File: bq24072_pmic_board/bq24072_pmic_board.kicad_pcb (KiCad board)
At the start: 2 copper layers, 40 x 20 mm, 28 parts, among them J101 USB_B_Micro, J102 Battery, J103 Conn_01x04_Female, U101 BQ24072RGT, U102 AMS1117-3.3

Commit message: WIP
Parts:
- removed JP101, JP102: SolderJumper_2_Open, Jumper:SolderJumper-2_P1.3mm_Open_RoundedPad1.0x1.5mm
- added JP1: SolderJumper_2_Open, Jumper:SolderJumper-2_P1.3mm_Open_RoundedPad1.0x1.5mm, F.Cu at (128.4, 97.2)
- added JP2: SolderJumper_2_Open, Jumper:SolderJumper-2_P1.3mm_Open_RoundedPad1.0x1.5mm, F.Cu at (128.4, 82.8)
- moved TP103 11.4 mm to (146.0, 86.0)
- moved J102 4.88 mm to (144.0, 93.5), turned to 0 degrees
- moved TP105 1.80 mm to (152.0, 96.6)
- moved REF** 0.20 mm to (158.0, 97.0)
- moved REF** 0.20 mm to (158.0, 83.0)
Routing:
- net Net-(C102-Pad2): track 35.5 -> 32.1 mm, vias 6 -> 4
- net Net-(J101-Pad6): track 16.9 -> 19.3 mm
- net GND: track 22.5 -> 24.5 mm, vias 14 -> 15
- net 3V3: track 22.1 -> 23.9 mm
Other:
- board text added: "+"
- board text added: "BAT"
- board text added: "V1"
- board text removed: "v1"

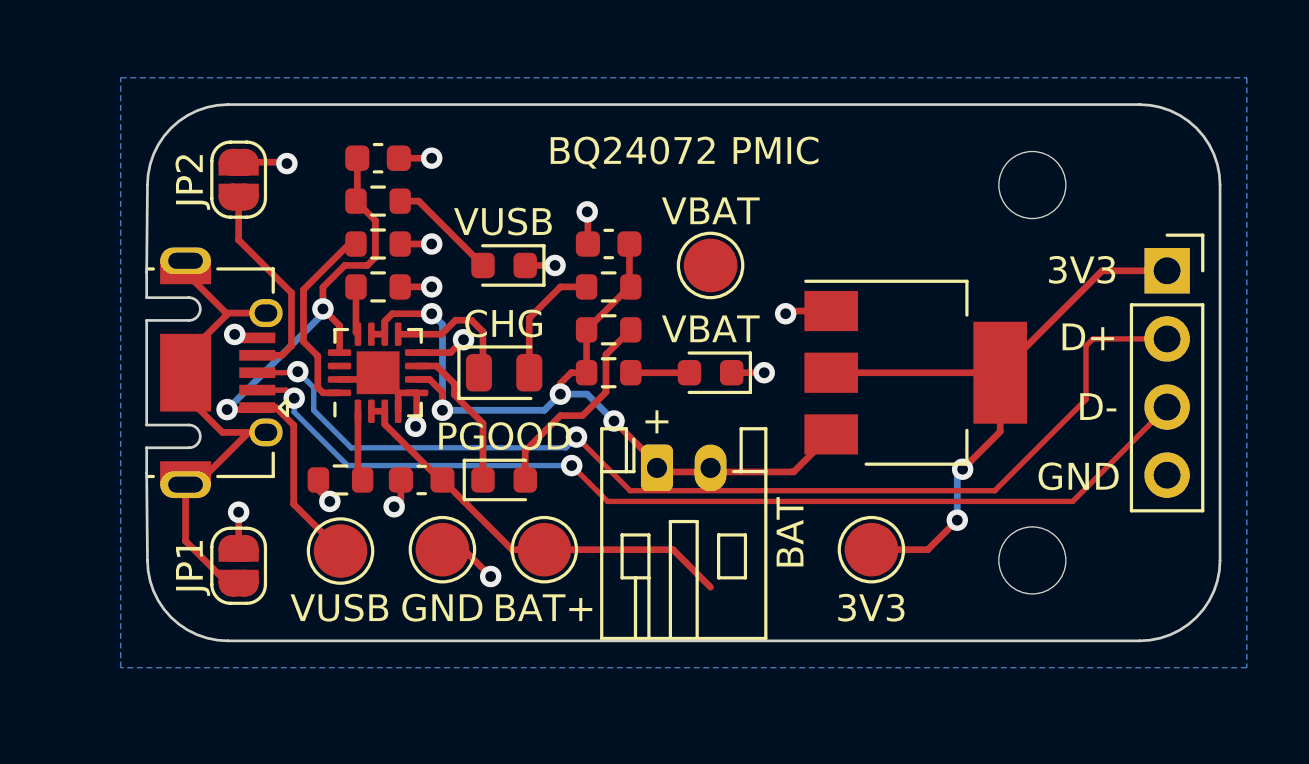
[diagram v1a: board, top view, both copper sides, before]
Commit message: [bq24072_pmic_board] Use hierarchical sheet for bq24072
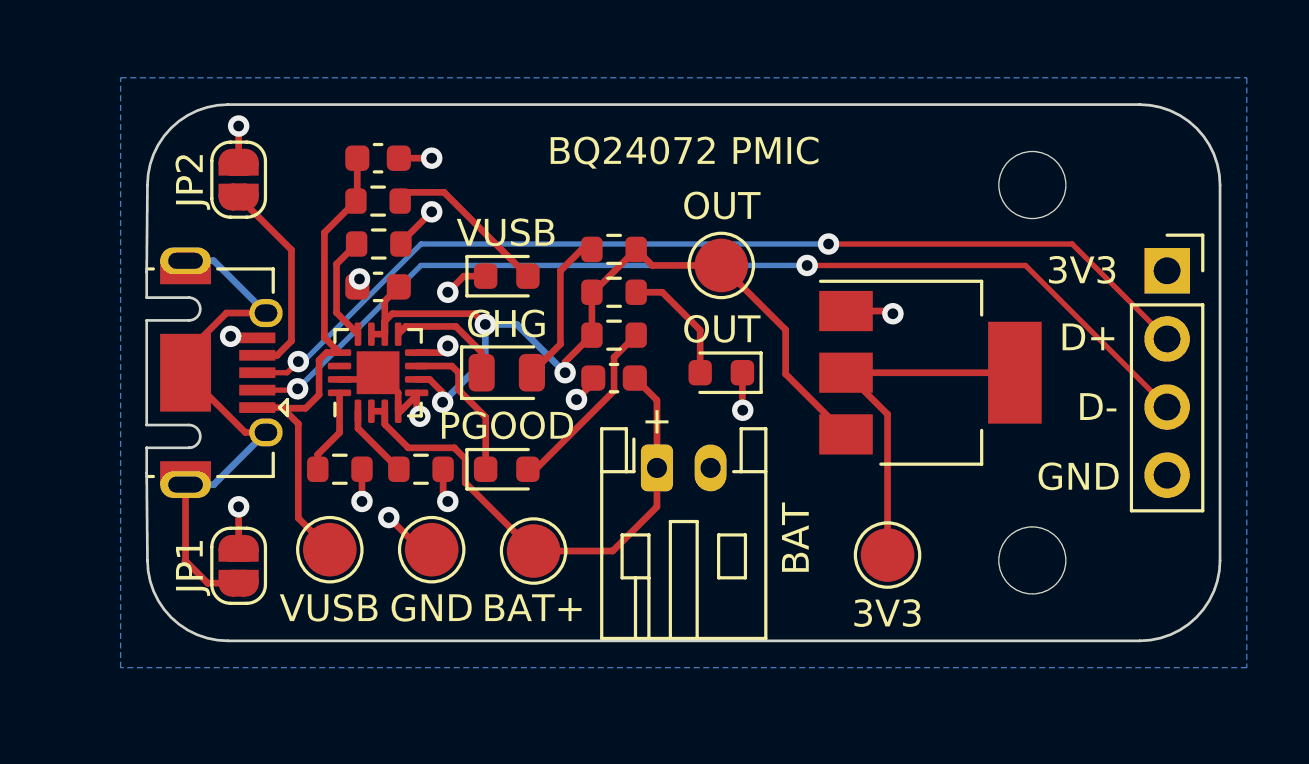
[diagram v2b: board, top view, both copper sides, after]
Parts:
- removed C101: 1u, Capacitor_SMD:C_0603_1608Metric
- removed C102, C103: 4.7u, Capacitor_SMD:C_0603_1608Metric
- removed D101: VUSB, LED_SMD:LED_0603_1608Metric
- removed D102: PGOOD, LED_SMD:LED_0603_1608Metric
- removed D103: CHG, LED_SMD:LED_0805_2012Metric
- removed D104: VBAT, LED_SMD:LED_0603_1608Metric
- removed R101: 180, Resistor_SMD:R_0603_1608Metric
- removed R102: 2k, Resistor_SMD:R_0603_1608Metric
- removed R103: 1k, Resistor_SMD:R_0603_1608Metric
- removed R104: 10k, Resistor_SMD:R_0603_1608Metric
- removed R105, R107: 47, Resistor_SMD:R_0603_1608Metric
- removed R106: 200, Resistor_SMD:R_0603_1608Metric
- removed TP105: 3V3, TestPoint:TestPoint_Pad_D2.0mm
- removed U102: AMS1117-3.3, Package_TO_SOT_SMD:SOT-223-3_TabPin2
- added C201: 1u, Capacitor_SMD:C_0603_1608Metric, F.Cu at (133.6, 82.0)
- added C202: 4.7u, Capacitor_SMD:C_0603_1608Metric, F.Cu at (133.6, 86.8)
- added C203: 4.7u, Capacitor_SMD:C_0603_1608Metric, F.Cu at (142.4, 90.2)
- added D201: VUSB, LED_SMD:LED_0603_1608Metric, F.Cu at (138.4, 86.4)
- added D202: PGOOD, LED_SMD:LED_0603_1608Metric, F.Cu at (138.4, 93.6)
- added D203: CHG, LED_SMD:LED_0805_2012Metric, F.Cu at (138.4, 90.0)
- added D204: OUT, LED_SMD:LED_0603_1608Metric, F.Cu at (146.4, 90.0)
- added R201: 180, Resistor_SMD:R_0603_1608Metric, F.Cu at (133.6, 83.6)
- added R202: 2k, Resistor_SMD:R_0603_1608Metric, F.Cu at (133.6, 85.2)
- added R203: 1k, Resistor_SMD:R_0603_1608Metric, F.Cu at (132.2, 93.6)
- added R204: 10k, Resistor_SMD:R_0603_1608Metric, F.Cu at (135.2, 93.6)
- added R205: 47, Resistor_SMD:R_0603_1608Metric, F.Cu at (142.4, 88.6)
- added R206: 200, Resistor_SMD:R_0603_1608Metric, F.Cu at (142.4, 85.4)
- added R207: 47, Resistor_SMD:R_0603_1608Metric, F.Cu at (142.4, 87.0)
- added TP201: VUSB, TestPoint:TestPoint_Pad_D2.0mm, F.Cu at (131.8, 96.6)
- added U201: BQ24072RGT, Package_DFN_QFN:VQFN-16-1EP_3x3mm_P0.5mm_EP1.6x1.6mm, F.Cu at (133.6, 90.0)
- TP101: value VUSB -> BAT+
- TP102: value BAT+ -> OUT
- TP103: value VBAT -> GND
- TP104: value GND -> 3V3
- U101: value BQ24072RGT -> AMS1117-3.3; footprint Package_DFN_QFN:VQFN-16-1EP_3x3mm_P0.5mm_EP1.6x1.6mm -> Package_TO_SOT_SMD:SOT-223-3_TabPin2
- moved U101 20.6 mm to (154.2, 90.0), turned to 0 degrees
- moved TP104 16.6 mm to (152.6, 96.8)
- moved TP103 14.8 mm to (135.6, 96.6), turned to 180 degrees
- moved TP102 12.5 mm to (146.4, 86.0)
- moved TP101 7.20 mm to (139.4, 96.7)
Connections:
- TP101 pad 1: VUSB -> BATT+
- TP102 pad 1: BATT+ -> OUT
- TP103 pad 1: Net-(C102-Pad2) -> GND
- TP104 pad 1: GND -> Net-(TP104-Pad1)
- U101 pad 1: Net-(R104-Pad2) -> GND
- U101 pad 2: BATT+ -> Net-(TP104-Pad1)
- U101 pad 3: BATT+ -> OUT
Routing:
- net OUT: track 0.00 -> 32.8 mm, vias 0 -> 3
- net Net-(C102-Pad2): track 32.1 -> 0.00 mm, vias 4 -> 0
- net 3V3: track 23.9 -> 0.00 mm, vias 2 -> 0
- net Net-(TP104-Pad1): track 0.00 -> 13.7 mm
- net Net-(D102-Pad2): track 7.71 -> 0.00 mm
- net Net-(R103-Pad1): track 7.42 -> 0.00 mm
- net Net-(D202-Pad2): track 0.00 -> 6.84 mm
- net Net-(D201-Pad2): track 0.00 -> 6.19 mm
- net Net-(D203-Pad2): track 0.00 -> 5.75 mm
- net Net-(D102-Pad1): track 5.71 -> 0.00 mm
- net Net-(D202-Pad1): track 0.00 -> 5.69 mm
- net Net-(D103-Pad1): track 5.14 -> 0.00 mm
- net Net-(D103-Pad2): track 4.66 -> 0.00 mm
- net Net-(D204-Pad2): track 0.00 -> 4.56 mm
- net Net-(D203-Pad1): track 0.00 -> 4.39 mm
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
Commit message: [bq24072_pmic_board] Move some LEDs from the hierarchical sheet
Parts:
- removed D201: VUSB, LED_SMD:LED_0603_1608Metric
- removed D204: OUT, LED_SMD:LED_0603_1608Metric
- removed R201: 180, Resistor_SMD:R_0603_1608Metric
- removed R207: 47, Resistor_SMD:R_0603_1608Metric
- added D101: VUSB, LED_SMD:LED_0603_1608Metric, F.Cu at (138.4, 86.4)
- added D102: VBAT, LED_SMD:LED_0603_1608Metric, F.Cu at (146.4, 90.0)
- added R101: 180, Resistor_SMD:R_0603_1608Metric, F.Cu at (133.6, 83.6)
- added R102: 47, Resistor_SMD:R_0603_1608Metric, F.Cu at (142.4, 87.0)
- moved TP104 1.02 mm to (153.6, 96.6)
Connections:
- TP104 pad 1: Net-(TP104-Pad1) -> 3V3
- U101 pad 2: Net-(TP104-Pad1) -> 3V3
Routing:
- net 3V3: track 0.00 -> 21.5 mm, vias 0 -> 1
- net Net-(TP104-Pad1): track 13.7 -> 0.00 mm
- net Net-(D201-Pad2): track 6.19 -> 0.00 mm
- net Net-(D101-Pad2): track 0.00 -> 6.19 mm
- net Net-(D204-Pad2): track 4.56 -> 0.00 mm
- net Net-(D102-Pad2): track 0.00 -> 4.56 mm

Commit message: final touches + v1 jlcpcb fab files
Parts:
- removed TP201: VUSB, TestPoint:TestPoint_Pad_D2.0mm
- added TP105: VUSB, TestPoint:TestPoint_Pad_D2.0mm, F.Cu at (132.0, 96.6)
- D102: value VBAT -> OUT
- R101: value 180 -> 1k
- R102, R205: value 47 -> 1k
- R206: value 200 -> 1k

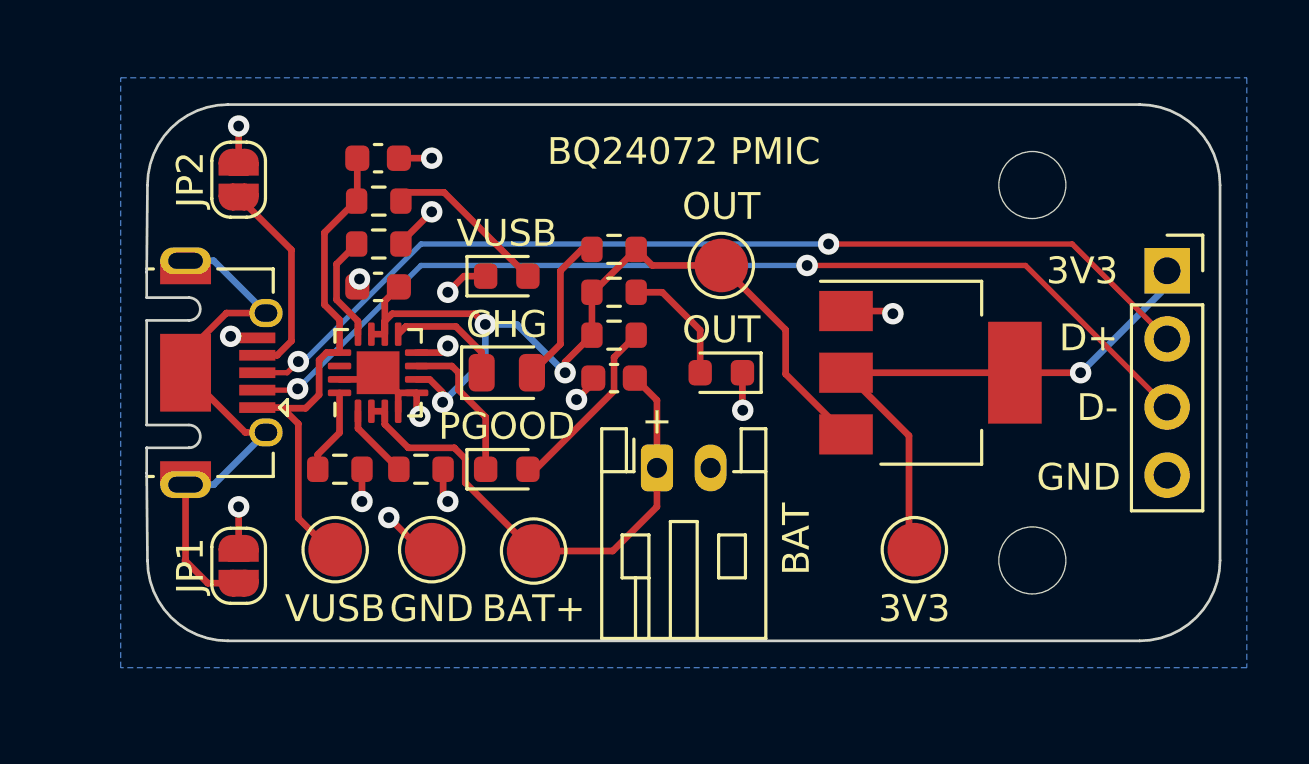
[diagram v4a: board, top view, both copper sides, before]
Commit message: [bq24072_pmic_board] Add VBUS output and bump board revision to v2
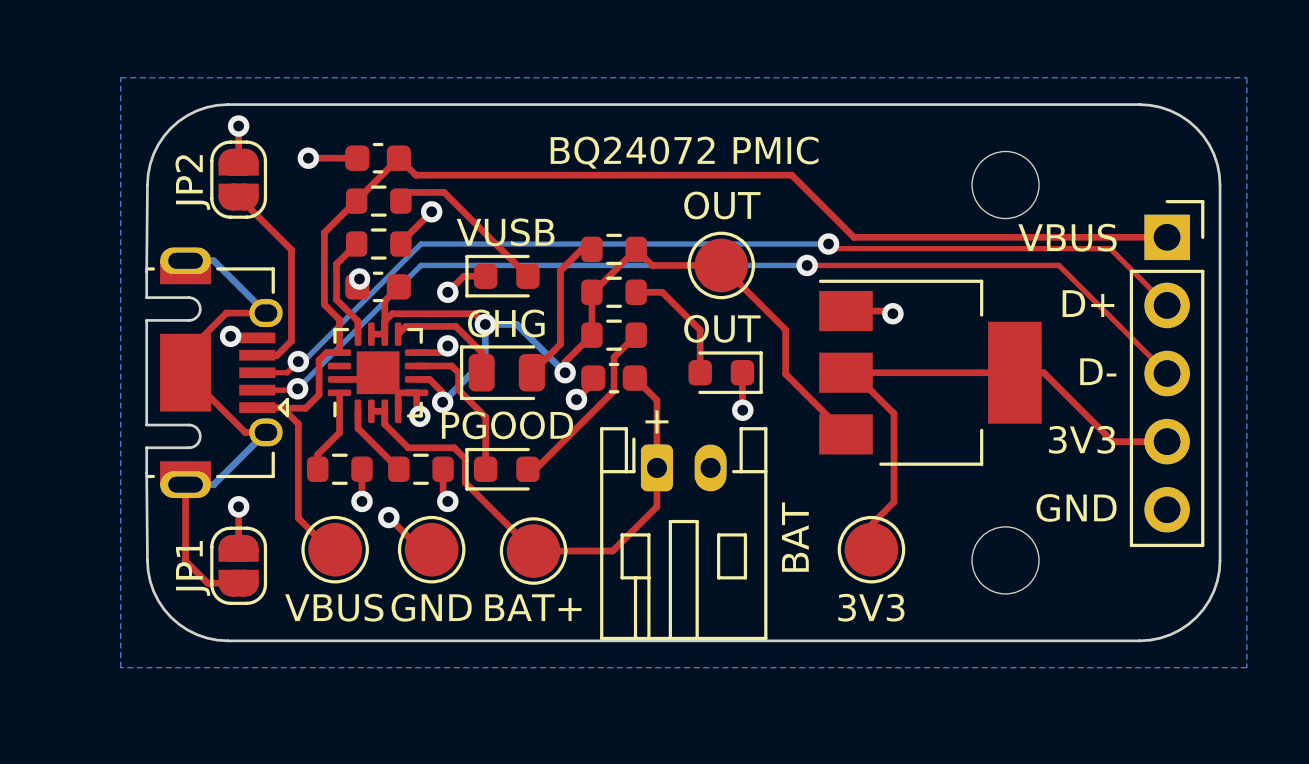
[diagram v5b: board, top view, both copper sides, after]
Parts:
- J103: value Conn_01x04_Female -> Conn_01x05_Female; footprint Connector_PinSocket_2.54mm:PinSocket_1x04_P2.54mm_Vertical -> Connector_PinSocket_2.54mm:PinSocket_1x05_P2.54mm_Vertical
- TP105: value VUSB -> VBUS
- moved TP104 1.60 mm to (152.0, 96.6)
- moved J103 1.25 mm to (163.0, 85.0)
- moved REF** 1.00 mm to (157.0, 97.0)
- moved REF** 1.00 mm to (157.0, 83.0)
- turned C201 to 180 degrees
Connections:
- C201 pad 1: VUSB -> VBUS
- J101 pad 1: VUSB -> VBUS
- J103 pad 1: 3V3 -> VBUS
- J103 pad 4: GND -> 3V3
- R101 pad 2: VUSB -> VBUS
- TP105 pad 1: VUSB -> VBUS
- U201 pad 13: VUSB -> VBUS
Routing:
- net VBUS: track 0.00 -> 49.3 mm
- net VUSB: track 18.7 -> 0.00 mm
- net GND: track 23.8 -> 24.6 mm
- net 3V3: track 21.5 -> 20.9 mm, vias 1 -> 0
- net D-: track 38.0 -> 37.5 mm
- net D+: track 37.4 -> 36.9 mm
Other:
- board text added: "V2"
- board text added: "VBUS"
- board text removed: "V1"

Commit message: [bq24072_pmic_board] V2 JLCPCB fab files
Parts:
- TP105: value VBUS -> VUSB
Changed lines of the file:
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@@
       (layerselection 0x00010fc_ffffffff)
       (disableapertmacros false)
-      (usegerberextensions false)
+      (usegerberextensions true)
       (usegerberattributes true)
-      (usegerberadvancedattributes true)
-      (creategerberjobfile true)
+      (usegerberadvancedattributes false)
+      (creategerberjobfile false)
       (svguseinch false)
       (svgprecision 6)
@@
       (plotinvisibletext false)
       (sketchpadsonfab false)
-      (subtractmaskfromsilk false)
+      (subtractmaskfromsilk true)
       (outputformat 1)
       (mirror false)
       (drillshape 0)
       (scaleselection 1)
-      (outputdirectory "fab/v1/jlcpcb")
+      (outputdirectory "fab/v2/jlcpcb")
     )
   )
@@
       (effects (font (size 1 1) (thickness 0.15)))
     )
-    (fp_text value "VBUS" (at 0 2.2) (layer "F.SilkS")
+    (fp_text value "VUSB" (at 0 2.2) (layer "F.SilkS")
       (effects (font (size 1 1) (thickness 0.15)))
     )
